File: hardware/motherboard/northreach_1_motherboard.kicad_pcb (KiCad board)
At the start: 2 copper layers, 41 x 96 mm, 22 parts, among them J1 USB_C_Receptacle, J2 Conn_01x03_Pin, J3 Conn_01x20, J4 Conn_01x03_Pin, SW1 SW_Push, SW2 SW_Push, U1 TPS7A4701xRGW, U2 ESP32-S3-MINI-1U, U3 USBLC6-2SC6

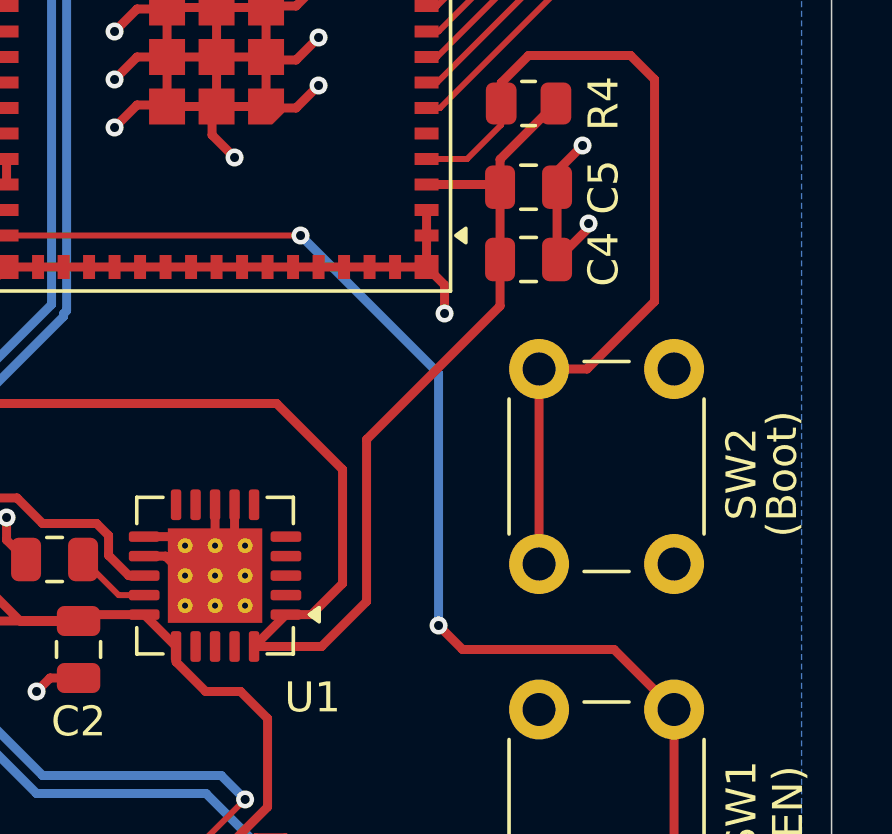
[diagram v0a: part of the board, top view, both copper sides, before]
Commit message: schematic_and_pcb: motherboard: route SENSE VREG pin to load
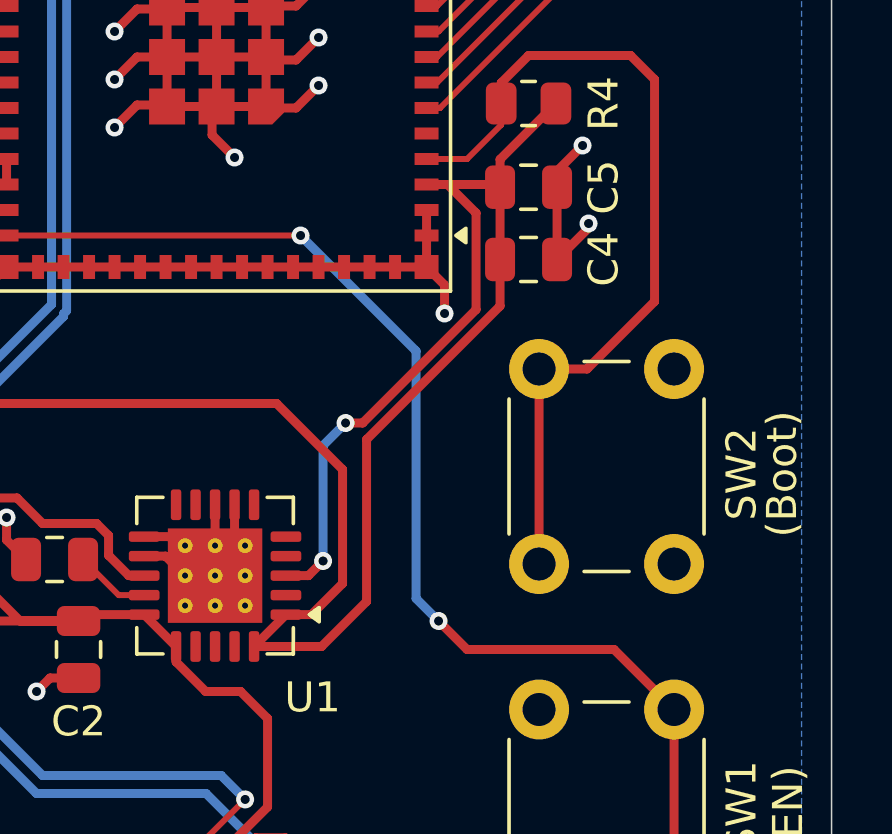
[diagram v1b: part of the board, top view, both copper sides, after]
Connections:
- U1 pad 3: unconnected-(U1-SENSE/FB-Pad3) -> VDD
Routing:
- net VDD: track 107.0 -> 124.5 mm, vias 0 -> 2
